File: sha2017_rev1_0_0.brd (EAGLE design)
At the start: 95 x 86 mm, 201 parts, among them IC1 CP210X_USB_UART, IC2 AP7215, IC3 ESP32WROOM32, IC4 TP4056, M1 MOTOR10MM, Q1 MMBT2222A, Q2 MMBT2222A, Q3 MMBT2222A, Q4 MMBT2222A, Q5 SI1304 BDL, Q6 MMBT2222A, U1 MPR121QR2, X2 2908-05WB-MG, X4 JST-PH3

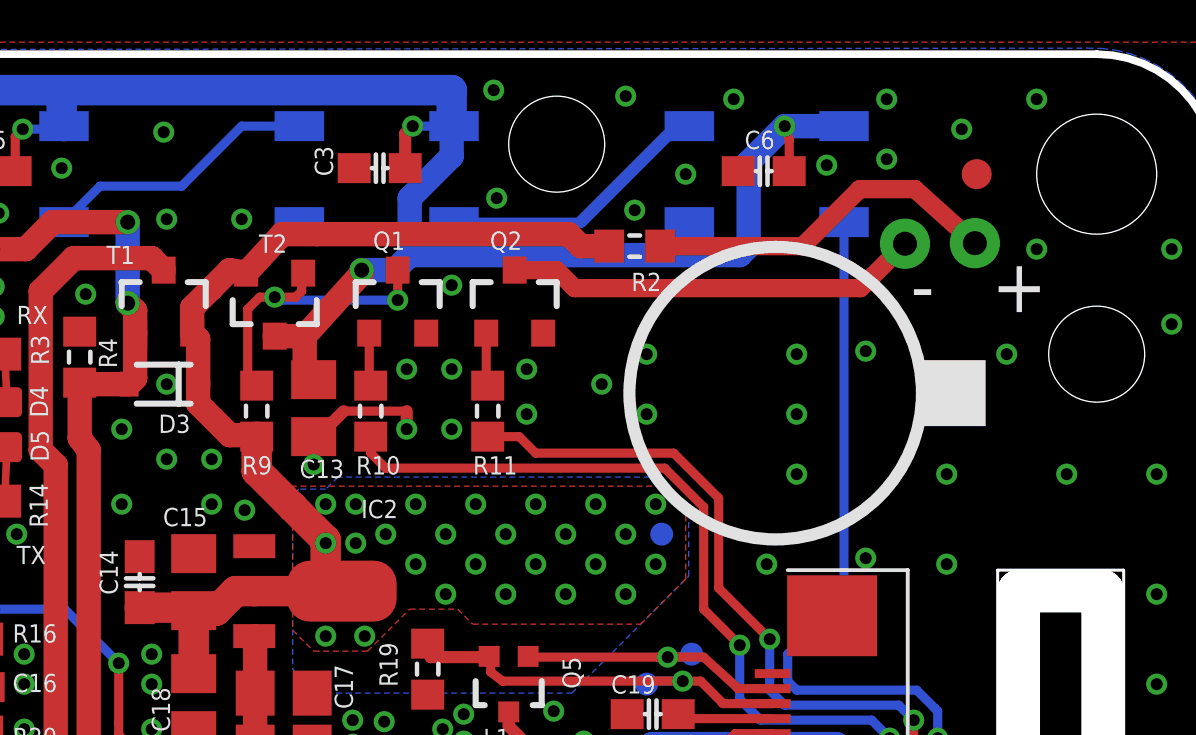
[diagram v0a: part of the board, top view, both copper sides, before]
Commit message: R2 0603->1206
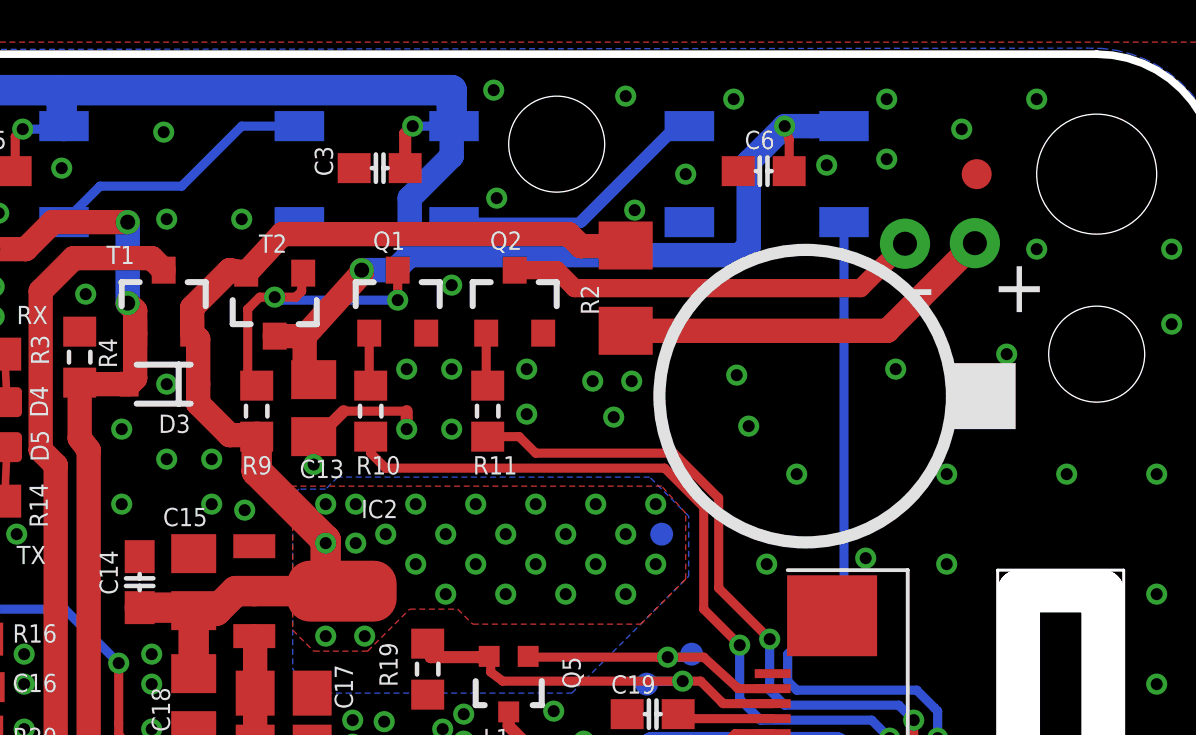
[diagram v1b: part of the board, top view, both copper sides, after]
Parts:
- R2: device 00ralf:R0603-DASHES -> resistor:R1206
- moved R2 1.43 mm to (75.3, 77.2), turned to 90 degrees
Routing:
- net N$18: track 12.0 -> 12.9 mm
- net VCC: track 38.7 -> 39.3 mm
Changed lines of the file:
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@@
 <wire x1="18.2" y1="1" x2="76.7" y2="0.9" width="0.4064" layer="21"/>
 <wire x1="18.2" y1="40.6" x2="18.2" y2="1" width="0.4064" layer="21"/>
-<circle x="80.3" y="73.7" radius="4.875446875" width="0.4064" layer="21"/>
-<rectangle x1="85.2" y1="72.6" x2="87.3" y2="74.8" layer="21"/>
+<circle x="81.3" y="73.6" radius="4.875446875" width="0.4064" layer="21"/>
+<rectangle x1="86.2" y1="72.5" x2="88.3" y2="74.7" layer="21"/>
 <text x="87.5" y="76.4" size="1.778" layer="21" font="vector" ratio="16">+</text>
 <text x="84.8" y="76.4" size="1.778" layer="21" font="vector" ratio="16">-</text>
@@
 <attribute name="PARTNO" value="BC817-25,215" x="71.6" y="76.7" size="1.778" layer="27" display="off"/>
 </element>
-<element name="R2" library="00ralf" package="R0603-DASHES" value="27R" x="75.6" y="78.6" smashed="yes" rot="R180">
-<attribute name="NAME" x="76.489" y="77.711" size="0.6096" layer="25" font="vector" ratio="16" rot="R180"/>
-<attribute name="VALUE" x="76.489" y="80.632" size="1.27" layer="27" rot="R180"/>
-<attribute name="PARTNO" value="ERJ-3GEYJ220V" x="75.6" y="78.6" size="1.778" layer="27" rot="R180" display="off"/>
+<element name="R2" library="resistor" package="R1206" value="27R" x="75.3" y="77.2" smashed="yes" rot="R90">
+<attribute name="NAME" x="74.411" y="76.311" size="0.6096" layer="25" font="vector" ratio="16" rot="R90"/>
+<attribute name="VALUE" x="77.332" y="76.311" size="1.27" layer="27" rot="R90"/>
+<attribute name="PARTNO" value="ERJ-3GEYJ220V" x="75.3" y="77.2" size="1.778" layer="27" rot="R90" display="off"/>
 </element>
 <element name="R11" library="00ralf" package="R0603-DASHES" value="10k" x="70.7" y="73.1" smashed="yes" rot="R270">
@@
 <via x="72" y="74.5" extent="1-16" drill="0.4"/>
 <via x="72" y="73" extent="1-16" drill="0.4"/>
-<via x="74.5" y="74" extent="1-16" drill="0.4"/>
+<via x="74.2" y="74.1" extent="1-16" drill="0.4"/>
 <via x="59.5" y="62.5" extent="1-16" drill="0.4"/>
 <via x="59.5" y="65" extent="1-16" drill="0.4"/>
@@
 <via x="22" y="71" extent="1-16" drill="0.4"/>
 <via x="28.5" y="68.7" extent="1-16" drill="0.4"/>
-<via x="76" y="75" extent="1-16" drill="0.4"/>
-<via x="81" y="75" extent="1-16" drill="0.4"/>
-<via x="76" y="73" extent="1-16" drill="0.4"/>
-<via x="81" y="73" extent="1-16" drill="0.4"/>
+<via x="75.5" y="74.1" extent="1-16" drill="0.4"/>
+<via x="79" y="74.3" extent="1-16" drill="0.4"/>
+<via x="74.9" y="72.9" extent="1-16" drill="0.4"/>
+<via x="79.4" y="72.6" extent="1-16" drill="0.4"/>
 <via x="81" y="71" extent="1-16" drill="0.4"/>
 <via x="80" y="68" extent="1-16" drill="0.4"/>
-<via x="83.3" y="75.1" extent="1-16" drill="0.4"/>
+<via x="84.3" y="74.5" extent="1-16" drill="0.4"/>
 <via x="88" y="75" extent="1-16" drill="0.4"/>
 <via x="86" y="71" extent="1-16" drill="0.4"/>
@@
 <wire x1="65.5" y1="67.1" x2="65.84" y2="67.1" width="0.6096" layer="1"/>
 <contactref element="R2" pad="2"/>
-<wire x1="61.5" y1="77.2" x2="62.1" y2="77.8" width="0.8128" layer="1"/>
-<wire x1="65" y1="79" x2="73.4" y2="79" width="0.8128" layer="1"/>
+<wire x1="63.85" y1="79" x2="73.4" y2="79" width="0.8128" layer="1"/>
 <wire x1="73.4" y1="79" x2="73.8" y2="78.6" width="0.8128" layer="1"/>
-<wire x1="73.8" y1="78.6" x2="74.75" y2="78.6" width="0.8128" layer="1"/>
 <wire x1="63" y1="72.25" x2="62.95" y2="72.25" width="0.6096" layer="1"/>
 <wire x1="63" y1="72.25" x2="63" y2="71.1" width="1.016" layer="1"/>
-<wire x1="63" y1="71.1" x2="64.2" y2="69.9" width="1.016" layer="1"/>
-<wire x1="64.2" y1="69.9" x2="65.3" y2="68.8" width="1.016" layer="1"/>
+<wire x1="63" y1="71.1" x2="65.3" y2="68.8" width="1.016" layer="1"/>
 <wire x1="65.3" y1="68.8" x2="65.3" y2="67.1" width="1.016" layer="1"/>
 <wire x1="62.9188" y1="67.1" x2="65.5" y2="67.1" width="1.016" layer="1"/>
@@
 <contactref element="TP129" pad="P$1"/>
 <contactref element="T2" pad="2"/>
-<wire x1="65" y1="79" x2="63.85" y2="79" width="0.8128" layer="1"/>
 <wire x1="63.85" y1="79" x2="62.65" y2="77.7" width="0.8128" layer="1"/>
 <wire x1="62.1" y1="77.8" x2="62.65" y2="77.7" width="0.8128" layer="1"/>
-<wire x1="61.5" y1="77.2" x2="60.85" y2="76.55" width="0.8128" layer="1"/>
+<wire x1="62.1" y1="77.8" x2="60.85" y2="76.55" width="0.8128" layer="1"/>
 <wire x1="60.85" y1="76.55" x2="60.85" y2="75.7" width="0.8128" layer="1"/>
 <wire x1="60.85" y1="75.7" x2="61.05" y2="75.5" width="0.8128" layer="1"/>
@@
 <wire x1="62.1" y1="72.3" x2="62.95" y2="72.3" width="0.8128" layer="1"/>
 <wire x1="62.95" y1="72.3" x2="63" y2="72.25" width="0.8128" layer="1"/>
+<wire x1="73.8" y1="78.6" x2="75.278" y2="78.6" width="0.8128" layer="1"/>
+<wire x1="75.278" y1="78.6" x2="75.3" y2="78.622" width="0.8128" layer="1"/>
 </signal>
 <signal name="VIBRATOR">
@@
 <contactref element="R2" pad="1"/>
 <contactref element="M1" pad="+"/>
-<wire x1="76.45" y1="78.6" x2="81.2" y2="78.6" width="0.6096" layer="1"/>
-<wire x1="81.2" y1="78.6" x2="83.1" y2="80.5" width="0.6096" layer="1"/>
-<wire x1="83.1" y1="80.5" x2="84.94" y2="80.5" width="0.6096" layer="1"/>
-<wire x1="84.94" y1="80.5" x2="86.94" y2="78.7" width="0.6096" layer="1"/>
+<wire x1="75.3" y1="75.778" x2="84.018" y2="75.778" width="0.8128" layer="1"/>
+<wire x1="84.018" y1="75.778" x2="86.94" y2="78.7" width="0.8128" layer="1"/>
 </signal>
 <signal name="WS2812_DATA_OUT">

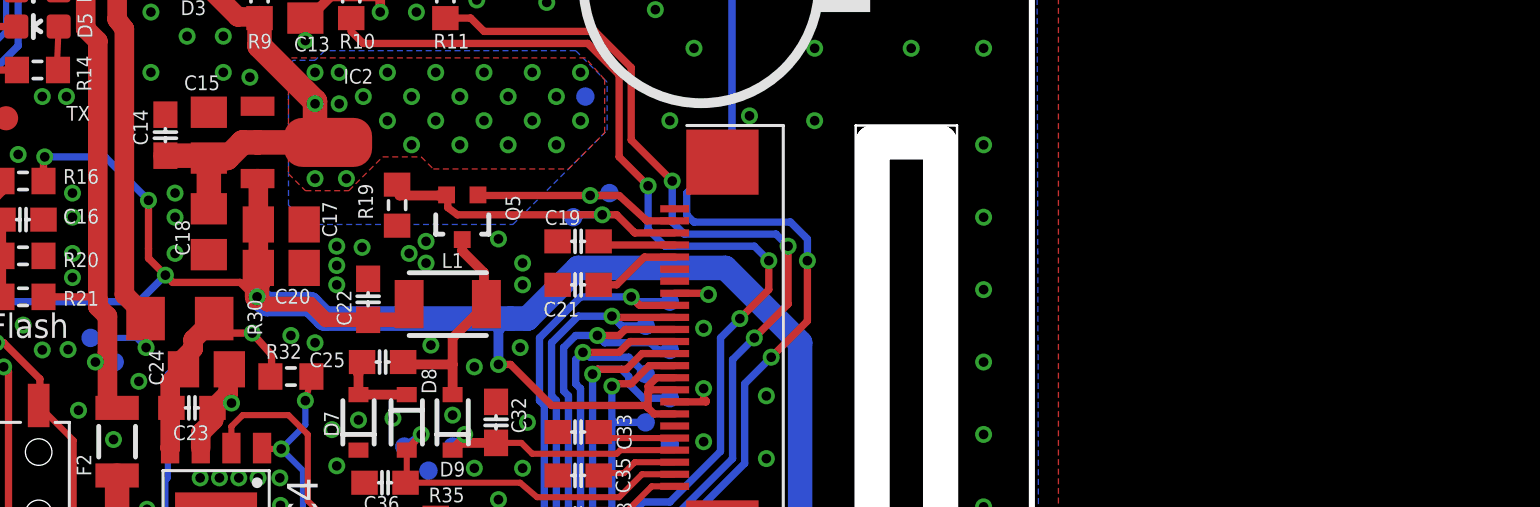
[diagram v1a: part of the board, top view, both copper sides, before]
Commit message: Extra vreg (not routed\!)
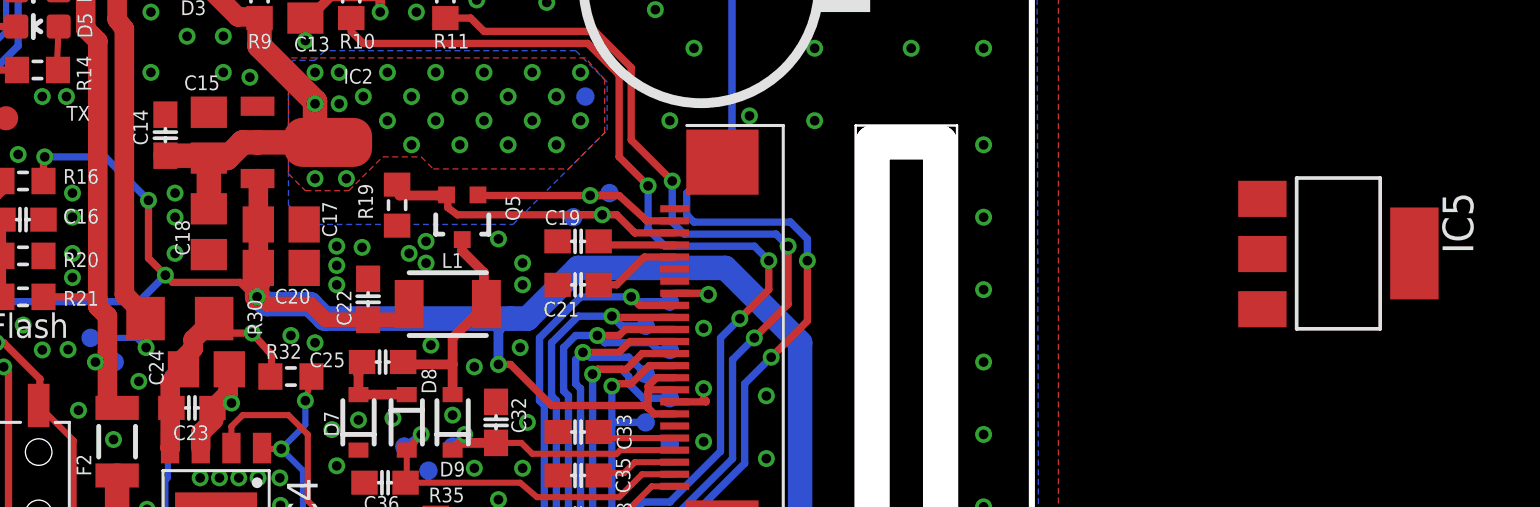
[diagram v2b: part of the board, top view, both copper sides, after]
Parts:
- added IC5: AMS1117, burr-brown:SOT223
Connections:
- net +3V3: now also IC5.2
- net GND: now also IC5.1
- net VCC: now also IC5.3

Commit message: Replace vreg
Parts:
- removed IC5: AMS1117, burr-brown:SOT223
- IC2: value AP7215 -> LD117AS33TR; device badge:SOT89 -> v-reg:SOT223
- R2: device resistor:R1206 -> rcl:R1206
- moved TP129 17.9 mm to (61.4, 78.7)
- moved R2 2.30 mm to (76.6, 79.1), turned to 180 degrees
- moved C14 1.61 mm to (59.9, 68.8), turned to 180 degrees
- moved C17 1.53 mm to (63.1, 62.4), turned to 270 degrees
- moved IC2 1.50 mm to (66.1, 68.0)
- moved C20 1.12 mm to (64.9, 62.4), turned to 270 degrees
- moved C15 1.08 mm to (59.9, 67.0), turned to 180 degrees
- moved R19 0.81 mm to (69.4, 64.1)
- moved C13 0.32 mm to (65.2, 73.3)
- moved R9 0.20 mm to (63.0, 73.3)
- moved R10 0.14 mm to (66.9, 73.2)
- moved C19 0.10 mm to (76.3, 63.0)
- moved C21 0.10 mm to (76.3, 61.2)
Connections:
- net +3V3: now also IC2.4; no longer IC2.3, IC5.2
- net GND: no longer IC5.1
- net VCC: now also IC2.3; no longer IC2.2, IC2.2@, IC5.3
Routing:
- net +3V3: track 225.2 -> 233.0 mm, vias 8 -> 32
- net VCC: track 39.3 -> 36.2 mm, vias 25 -> 1
- net N$18: track 12.9 -> 10.2 mm
- net WS2812_POWER: track 155.3 -> 153.8 mm
- net RESE: track 14.4 -> 13.4 mm
- net GND: track 41.9 -> 42.1 mm, vias 298 -> 303
- added copper zone on layer 1, net +3V3
- added copper zone on layer 16, net +3V3
- removed copper zone on layer 1, net VCC
- removed copper zone on layer 16, net VCC
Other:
- board text removed: "VCC"
